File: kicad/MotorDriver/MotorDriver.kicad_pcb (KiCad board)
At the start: 2 copper layers, 74 parts, among them J1 Conn_01x02_Socket, J2 Conn_01x03_Socket, U1 DRV8323RSRGZR, U2 CSD88599Q5DC, U3 CSD88599Q5DC, U5 CSD88599Q5DC, U6 STM32G474RETx

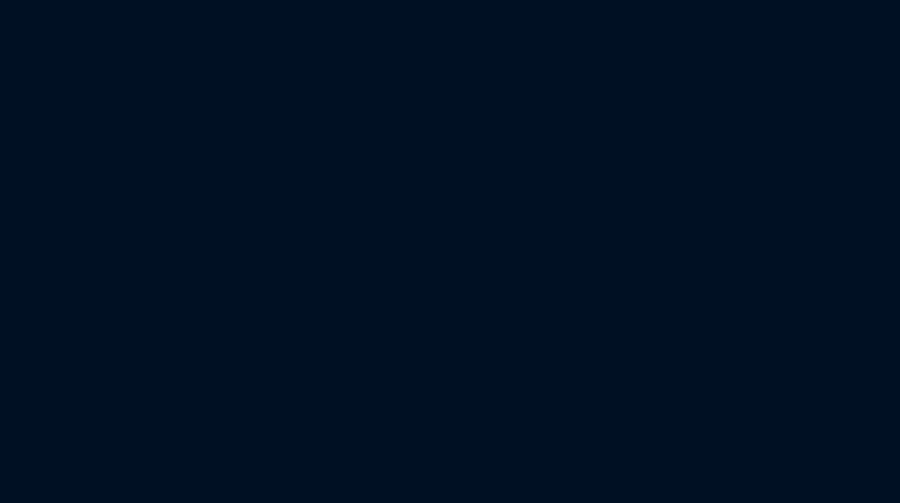
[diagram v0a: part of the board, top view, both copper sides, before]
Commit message: Good progress on the leg prototype. Looking at the jacobian project again, i think I can use some stuff from that project to help size the link lengths and also something to relate the tip forces to joint torques
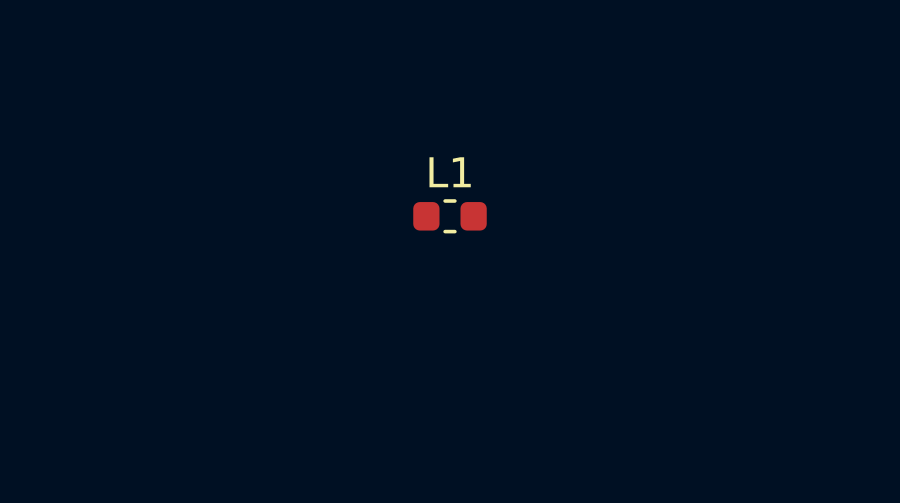
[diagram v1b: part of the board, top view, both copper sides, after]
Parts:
- added L1: L, Inductor_SMD:L_0603_1608Metric, F.Cu at (103.4, 61.0)
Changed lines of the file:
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@@
       (net 42 "/SHC") (pinfunction "2") (pintype "passive"))
+  )
+  (footprint "Inductor_SMD:L_0603_1608Metric" (layer "F.Cu")
+    (at 103.3525 60.96)
+    (descr "Inductor SMD 0603 (1608 Metric), square (rectangular) end terminal, IPC_7351 nominal, (Body size source: http://www.tortai-tech.com/upload/download/2011102023233369053.pdf), generated with kicad-footprint-generator")
+    (tags "inductor")
+    (property "Sheetfile" "MotorDriver.kicad_sch")
+    (property "Sheetname" "")
+    (property "ki_description" "Inductor")
+    (property "ki_keywords" "inductor choke coil reactor magnetic")
+    (attr smd)
+    (fp_text reference "L1" (at 0 -1.43) (layer "F.SilkS")
+        (effects (font (size 1 1) (thickness 0.15)))
+    )
+    (fp_text value "L" (at 0 1.43) (layer "F.Fab")
+        (effects (font (size 1 1) (thickness 0.15)))
+    )
+    (fp_text user "${REFERENCE}" (at 0 0) (layer "F.Fab")
+        (effects (font (size 0.4 0.4) (thickness 0.06)))
+    )
+    (fp_line (start -0.162779 -0.51) (end 0.162779 -0.51)
+      (stroke (width 0.12) (type solid)) (layer "F.SilkS"))
+    (fp_line (start -0.162779 0.51) (end 0.162779 0.51)
+      (stroke (width 0.12) (type solid)) (layer "F.SilkS"))
+    (fp_line (start -1.48 -0.73) (end 1.48 -0.73)
+      (stroke (width 0.05) (type solid)) (layer "F.CrtYd"))
+    (fp_line (start -1.48 0.73) (end -1.48 -0.73)
+      (stroke (width 0.05) (type solid)) (layer "F.CrtYd"))
+    (fp_line (start 1.48 -0.73) (end 1.48 0.73)
+      (stroke (width 0.05) (type solid)) (layer "F.CrtYd"))
+    (fp_line (start 1.48 0.73) (end -1.48 0.73)
+      (stroke (width 0.05) (type solid)) (layer "F.CrtYd"))
+    (fp_line (start -0.8 -0.4) (end 0.8 -0.4)
+      (stroke (width 0.1) (type solid)) (layer "F.Fab"))
+    (fp_line (start -0.8 0.4) (end -0.8 -0.4)
+      (stroke (width 0.1) (type solid)) (layer "F.Fab"))
+    (fp_line (start 0.8 -0.4) (end 0.8 0.4)
+      (stroke (width 0.1) (type solid)) (layer "F.Fab"))
+    (fp_line (start 0.8 0.4) (end -0.8 0.4)
+      (stroke (width 0.1) (type solid)) (layer "F.Fab"))
+    (pad "1" smd roundrect (at -0.7875 0) (size 0.875 0.95) (layers "F.Cu" "F.Paste" "F.Mask") (roundrect_rratio 0.25)
+      (net 48 "Net-(D4-K)") (pinfunction "1") (pintype "passive"))
+    (pad "2" smd roundrect (at 0.7875 0) (size 0.875 0.95) (layers "F.Cu" "F.Paste" "F.Mask") (roundrect_rratio 0.25)
+      (net 17 "+3.3V") (pinfunction "2") (pintype "passive"))
+    (model "${KICAD6_3DMODEL_DIR}/Inductor_SMD.3dshapes/L_0603_1608Metric.wrl"
+      (offset (xyz 0 0 0))
+      (scale (xyz 1 1 1))
+      (rotate (xyz 0 0 0))
+    )
   )
   (footprint "Diode_SMD:D_MELF" (layer "F.Cu")

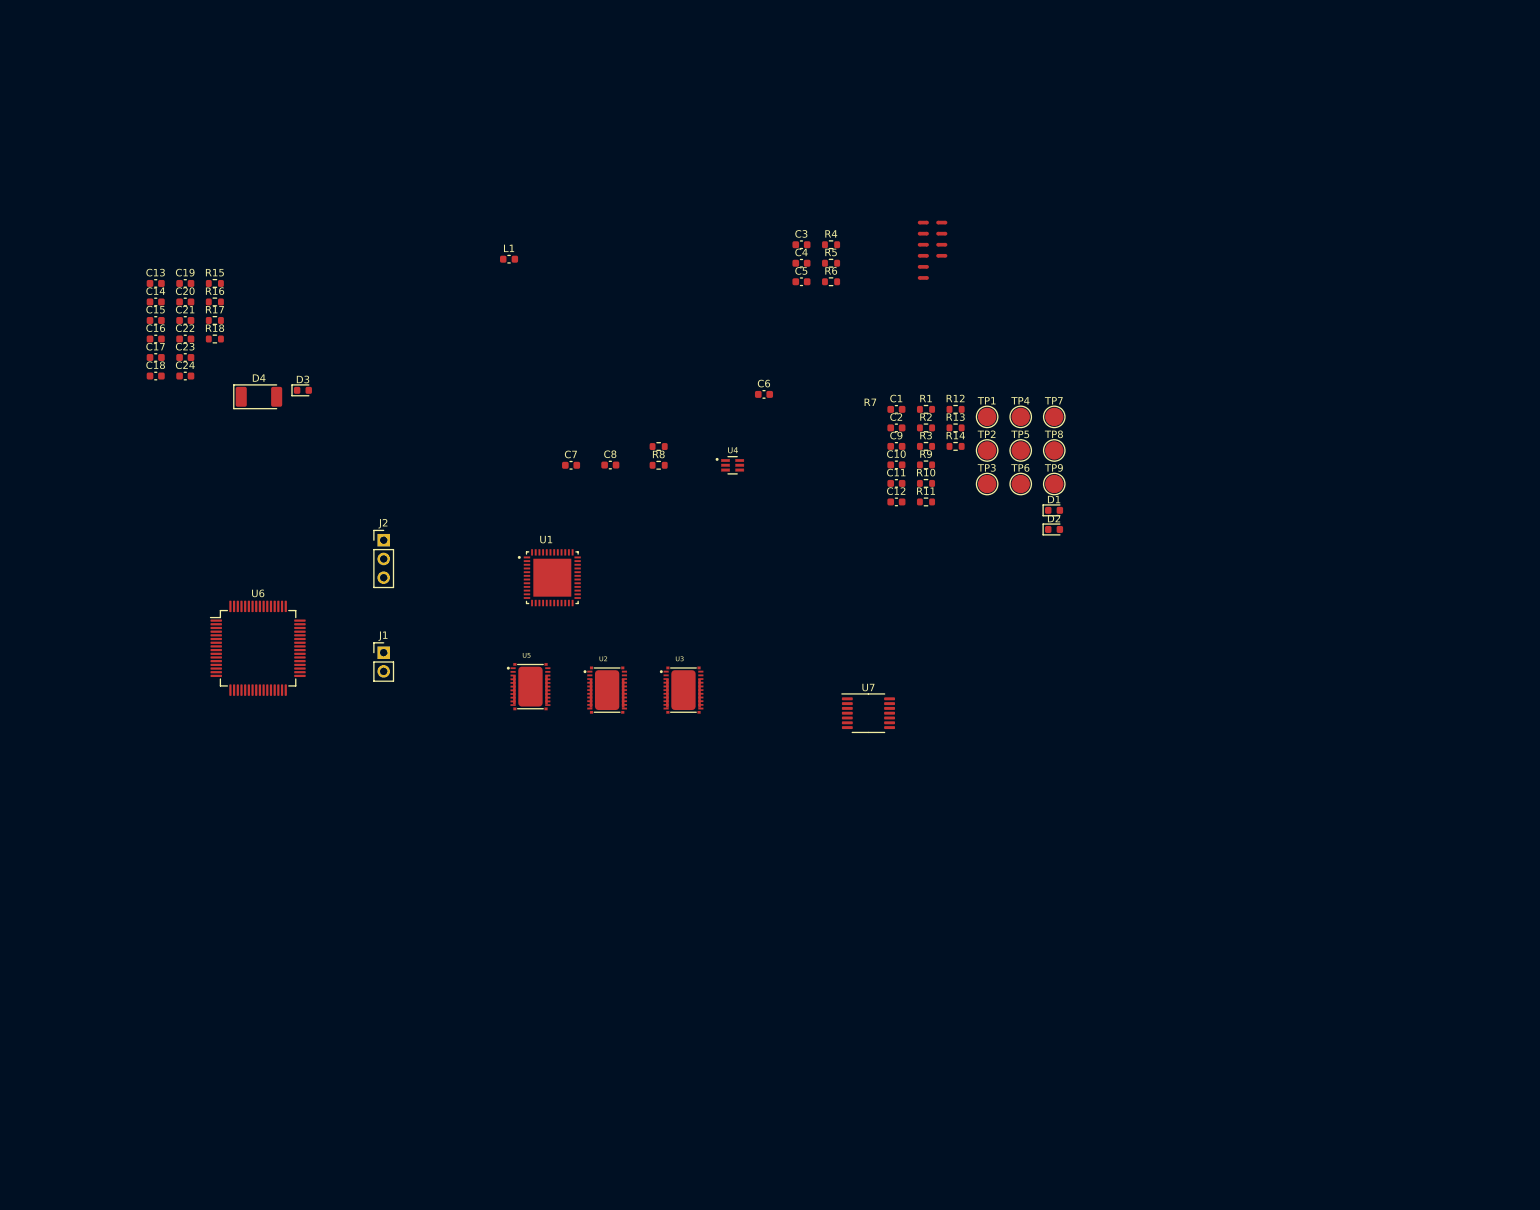
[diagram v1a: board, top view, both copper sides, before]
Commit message: Schematic capture is like 80% complete. There are some components that don't have appropriate footprints, IE the 330 mH caps. Started board layout. I'm not sure if I can fit everything in the current board outline though. I may need to expand to a full circle instead of having the cutout sections.
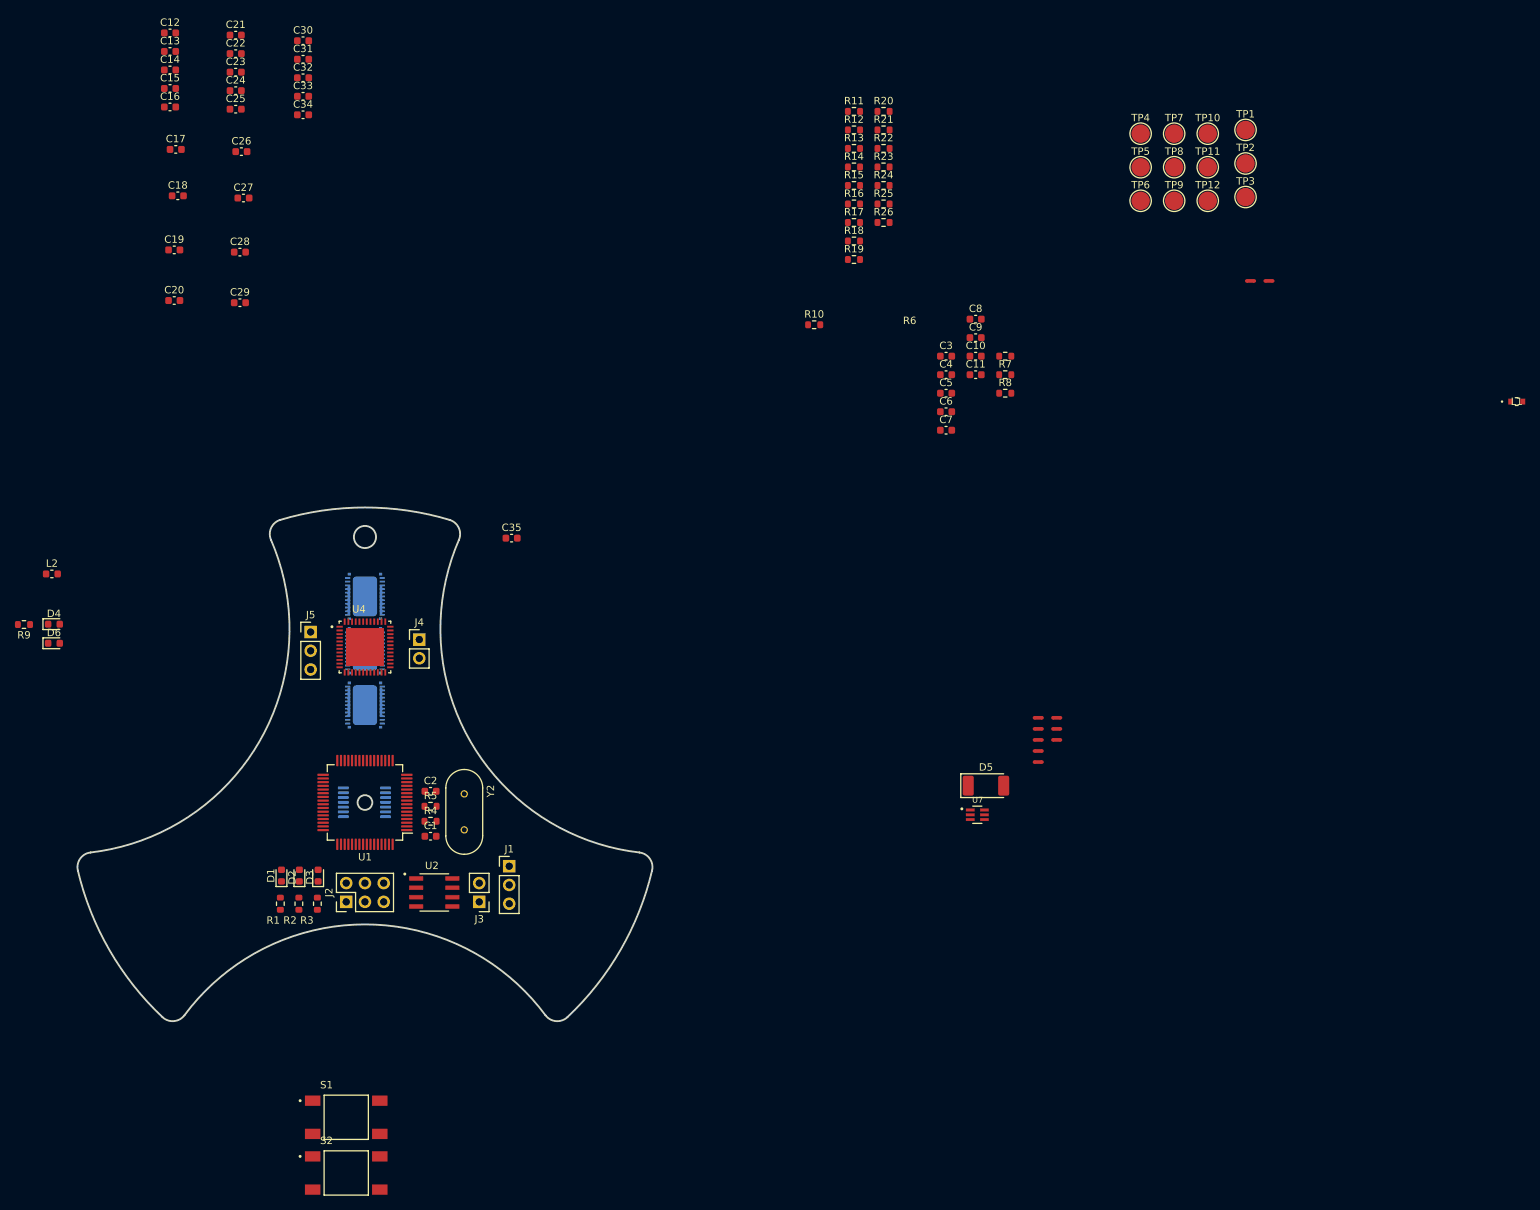
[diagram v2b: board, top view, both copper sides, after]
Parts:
- added C25: 0.1 uF, Capacitor_SMD:C_0603_1608Metric, F.Cu at (66.3, 40.6)
- added C26: 330uF, Capacitor_SMD:C_0603_1608Metric, F.Cu at (67.1, 46.4)
- added C27: 330uF, Capacitor_SMD:C_0603_1608Metric, F.Cu at (67.3, 52.7)
- added C28: 2200pF, Capacitor_SMD:C_0603_1608Metric, F.Cu at (66.9, 60.0)
- added C29: 2200pF, Capacitor_SMD:C_0603_1608Metric, F.Cu at (66.9, 66.9)
- added C30: 0.1uF, Capacitor_SMD:C_0603_1608Metric, F.Cu at (75.4, 31.3)
- added C31: 2200pF, Capacitor_SMD:C_0603_1608Metric, F.Cu at (75.4, 33.9)
- added C32: 0.01 uF, Capacitor_SMD:C_0603_1608Metric, F.Cu at (75.4, 36.4)
- added C33: 0.1 uF, Capacitor_SMD:C_0603_1608Metric, F.Cu at (75.4, 38.9)
- added C34: 0.01 uF, Capacitor_SMD:C_0603_1608Metric, F.Cu at (75.4, 41.4)
- added C35: 0.1 uF, Capacitor_SMD:C_0603_1608Metric, F.Cu at (103.7, 98.8)
- added D5: MBR1H100SFT3G, Diode_SMD:D_MELF, F.Cu at (168.0, 132.3)
- added D6: LED, LED_SMD:LED_0603_1608Metric, F.Cu at (41.7, 113.0)
- added J3: Conn_01x02_Pin, Connector_PinHeader_2.54mm:PinHeader_1x02_P2.54mm_Vertical, F.Cu at (99.3, 148.1)
- added J4: Conn_01x02_Socket, Connector_PinHeader_2.54mm:PinHeader_1x02_P2.54mm_Vertical, F.Cu at (91.2, 112.5)
- added J5: Conn_01x03_Socket, Connector_PinHeader_2.54mm:PinHeader_1x03_P2.54mm_Vertical, F.Cu at (76.5, 111.5)
- added L2: 15uH, Inductor_SMD:L_0603_1608Metric, F.Cu at (41.4, 103.6)
- added R19: 56, Resistor_SMD:R_0603_1608Metric, F.Cu at (150.1, 61.0)
- added R20: 56, Resistor_SMD:R_0603_1608Metric, F.Cu at (154.1, 40.9)
- added R21: 82.0k, Resistor_SMD:R_0603_1608Metric, F.Cu at (154.1, 43.4)
- added R22: 4.99k, Resistor_SMD:R_0603_1608Metric, F.Cu at (154.1, 45.9)
- added R23: 0.007, Resistor_SMD:R_0603_1608Metric, F.Cu at (154.1, 48.5)
- added R24: 82.0k, Resistor_SMD:R_0603_1608Metric, F.Cu at (154.1, 51.0)
- added R25: 4.99k, Resistor_SMD:R_0603_1608Metric, F.Cu at (154.1, 53.5)
- added R26: 0.007, Resistor_SMD:R_0603_1608Metric, F.Cu at (154.1, 56.0)
- added S1: TS04-66-75-BK-160-SMT, TylerLib:SW_TS04-66-75-BK-160-SMT, F.Cu at (81.3, 177.3)
- added S2: TS04-66-75-BK-160-SMT, TylerLib:SW_TS04-66-75-BK-160-SMT, F.Cu at (81.3, 184.8)
- added TP10: TestPoint, TestPoint:TestPoint_Pad_D2.5mm, F.Cu at (198.1, 43.9)
- added TP11: TestPoint, TestPoint:TestPoint_Pad_D2.5mm, F.Cu at (198.1, 48.5)
- added TP12: TestPoint, TestPoint:TestPoint_Pad_D2.5mm, F.Cu at (198.1, 53.0)
- added U8: CSD88599Q5DC, TylerLib:MOSFET_CSD88599Q5DC, B.Cu at (83.8, 121.4)
- added Y2: ABL-8.000MHZ-B1U-T, TylerLib:XTAL_ABL-8.000MHZ-B1U-T, F.Cu at (97.3, 135.9)
- C1: value 0.01 uF -> 18pF
- C10: value 0.1 uF -> 100nF
- C11: value 0.01 uF -> 100nF
- C12: value 0.1 uF -> 0.1uF
- C13: value 2.2uF -> 4.7uF
- C14: value 0.1uF -> 2.2uF
- C15, C21: value 1uF -> 0.1uF
- C16: value 0.047uF -> 1uF
- C18: value 1uF -> 0.047uF
- C19, C20, C22: value 1uF -> 1000pF
- C2: value 0.1 uF -> 18pF
- C23: value 1uF -> 22uF
- C24: value 22uF -> 0.01 uF
- C3, C4: value 330uF -> 100nF
- C5, C6, C8: value 2200pF -> 100nF
- C7: value 0.1uF -> 100nF
- C9: value 0.01 uF -> 4.7uF
- D4: value 1N6857UR -> LED; footprint Diode_SMD:D_MELF -> LED_SMD:LED_0603_1608Metric
- J1: value Conn_01x02_Socket -> Conn_01x03_Pin; footprint Connector_PinHeader_2.54mm:PinHeader_1x02_P2.54mm_Vertical -> Connector_PinHeader_2.54mm:PinHeader_1x03_P2.54mm_Vertical
- J2: value Conn_01x03_Socket -> Conn_01x06_Pin; footprint Connector_PinHeader_2.54mm:PinHeader_1x03_P2.54mm_Vertical -> Connector_PinHeader_2.54mm:PinHeader_2x03_P2.54mm_Vertical
- L1: value L -> MMZ1608B601CTAH0; footprint Inductor_SMD:L_0603_1608Metric -> TylerLib:IND_1608_TDK
- R1: value 82.0k -> 1k
- R10: value 4.99k -> 10k
- R11: value 0.007 -> 28.0k
- R12: value 82.0k -> 8.45k
- R13: value 4.99k -> 82.0k
- R14: value 0.007 -> 4.99k
- R15: value 330 -> 0.007
- R16: value 10k -> 82.0k
- R17: value 28.0k -> 4.99k
- R18: value 8.45k -> 56
- R2: value 4.99k -> 1k
- R3: value 0.007 -> 1k
- R4: value 82.0k -> 80
- R5: value 4.99k -> 80
- R6: value 56 -> 10k
- R7: value 56 -> 4.7k
- R8: value 56 -> 100
- R9: value 82.0k -> 330
- U1: value DRV8323RSRGZR -> STM32F446RETx; footprint TylerLib:QFN50P700X700X100-49N -> Package_QFP:LQFP-64_10x10mm_P0.5mm
- U2: value CSD88599Q5DC -> ATA6560-GAQW; footprint TylerLib:MOSFET_CSD88599Q5DC -> TylerLib:SOIC127P600X175-8N
- U3: value CSD88599Q5DC -> AS5147U; footprint TylerLib:MOSFET_CSD88599Q5DC -> Package_SO:TSSOP-14_4.4x5mm_P0.65mm; moved to B.Cu
- U4: value ~ -> DRV8323RSRGZR; footprint TylerLib:SOT65P210X110-6N -> TylerLib:QFN50P700X700X100-49N
- U5: moved to B.Cu
- U6: value STM32G474RETx -> CSD88599Q5DC; footprint Package_QFP:LQFP-64_10x10mm_P0.5mm -> TylerLib:MOSFET_CSD88599Q5DC; moved to B.Cu
- U7: footprint Package_SO:TSSOP-14_4.4x5mm_P0.65mm -> TylerLib:SOT65P210X110-6N
- moved L1 138.0 mm to (240.0, 80.3)
- moved R9 124.2 mm to (37.6, 110.5), turned to 180 degrees
- moved C12 117.2 mm to (57.4, 30.3)
- moved D1 115.9 mm to (72.5, 144.5), turned to 90 degrees
- moved D2 112.6 mm to (74.9, 144.5), turned to 90 degrees
- moved R1 110.2 mm to (72.3, 148.3), turned to -90 degrees
- moved R2 106.7 mm to (74.9, 148.3), turned to -90 degrees
- moved R3 103.2 mm to (77.4, 148.3), turned to -90 degrees
- moved R4 95.2 mm to (92.7, 137.2)
- moved R5 91.5 mm to (92.7, 135.1)
- moved R15 87.7 mm to (150.1, 51.0)
- moved R16 87.7 mm to (150.1, 53.5)
- moved R18 87.7 mm to (150.1, 58.5)
- moved R17 87.7 mm to (150.1, 56.0)
- moved C1 85.7 mm to (92.7, 139.2)
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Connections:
- C1 pad 1: Vdrive -> GND
- C1 pad 2: /SLA -> Net-(C1-Pad2)
- C10 pad 1: /VSENB -> Net-(C10-Pad1)
- C10 pad 2: GND -> /Microcontroller/NRST
- C11 pad 1: Vdrive -> Net-(C11-Pad1)
- C11 pad 2: /SLC -> /Microcontroller/Button
- C12 pad 1: /VSENC -> +3.3V
- C14 pad 1: +3.3V -> Vdrive
- C15 pad 1: Net-(U1-DVDD) -> Vdrive
- C16 pad 1: Net-(U1-CPH) -> Net-(U4-DVDD)
- C16 pad 2: Net-(U1-CPL) -> GND
- C17 pad 2: Net-(U1-VCP) -> Net-(U4-VCP)
- C18 pad 1: Vdrive -> Net-(U4-CPH)
- C18 pad 2: GND -> Net-(U4-CPL)
- C19 pad 1: Vdrive -> /MotorController/SPC
- C19 pad 2: GND -> /MotorController/SNC
- C2 pad 1: /VSENA -> GND
- C2 pad 2: GND -> Net-(C2-Pad2)
- C20 pad 1: /SPC -> /MotorController/SPA
- C20 pad 2: /SNC -> /MotorController/SNA
- C21 pad 1: /SPB -> Net-(U4-CB)
- C21 pad 2: /SNB -> Net-(D5-K)
- C22 pad 1: /SPA -> /MotorController/SPB
- C22 pad 2: /SNA -> /MotorController/SNB
- C23 pad 1: Net-(U1-CB) -> +3.3V
- C23 pad 2: Net-(D4-K) -> GND
- C24 pad 1: +3.3V -> Vdrive
- C24 pad 2: GND -> /MotorController/SLA
- C3 pad 1: Net-(J1-Pin_1) -> GND
- C3 pad 2: GND -> +3.3V
- C4 pad 1: Net-(J1-Pin_1) -> GND
- C4 pad 2: GND -> +3.3V
- C5 pad 1: /ISENA -> GND
- C5 pad 2: GND -> +3.3V
- C6 pad 1: /ISENB -> GND
- C6 pad 2: GND -> +3.3V
- C7 pad 1: Net-(C7-Pad1) -> GND
- C7 pad 2: GND -> +3.3V
- C8 pad 1: /ISENC -> GND
- C8 pad 2: GND -> +3.3V
- C9 pad 1: Vdrive -> GND
- C9 pad 2: /SLB -> Net-(U1-VCAP_1)
- D1 pad 1: GND -> Net-(D1-K)
- D1 pad 2: +3.3V -> Net-(D1-A)
- D2 pad 1: GND -> Net-(D2-K)
- D2 pad 2: /LED -> Net-(D2-A)
- D3 pad 2: +3.3V -> Net-(D3-A)
- D4 pad 2: GND -> +3.3V
- J1 pad 1: Net-(J1-Pin_1) -> GND
- J1 pad 2: GND -> /Microcontroller/UART_RX
- J2 pad 1: /MOTA -> /Microcontroller/NRST
- J2 pad 2: /MOTB -> /Microcontroller/TCK
- J2 pad 3: /MOTC -> /Microcontroller/TMS
- L1 pad 1: Net-(D4-K) -> Net-(U1-VDDA)
- NT1 pad 1: /SPA -> /MotorController/SPA
- NT1 pad 2: /SLA -> /MotorController/SLA
- NT10 pad 1: Net-(U5-SH) -> Net-(U8-SH)
- NT10 pad 2: /SHC -> /MotorController/SHC
- NT2 pad 1: /SNA -> /MotorController/SNA
- NT3 pad 1: Net-(U2-SH) -> Net-(U5-SH)
- NT3 pad 2: /SHA -> /MotorController/SHA
- NT4 pad 1: /VDRAIN -> /MotorController/VDRAIN
- NT5 pad 1: /SPB -> /MotorController/SPB
- NT5 pad 2: /SLB -> /MotorController/SLB
- NT6 pad 1: /SNB -> /MotorController/SNB
- NT7 pad 1: Net-(U3-SH) -> Net-(U6-SH)
- NT7 pad 2: /SHB -> /MotorController/SHB
- NT8 pad 1: /SPC -> /MotorController/SPC
- NT8 pad 2: /SLC -> /MotorController/SLC
- NT9 pad 1: /SNC -> /MotorController/SNC
- R1 pad 1: /MOTA -> Net-(D1-K)
- R1 pad 2: /VSENA -> GND
- R10 pad 1: /VSENB -> +3.3V
- R10 pad 2: GND -> /MotorController/nFault
- R11 pad 1: /SLB -> +3.3V
- R11 pad 2: GND -> Net-(U4-FB)
- R12 pad 1: /MOTC -> Net-(U4-FB)
- R12 pad 2: /VSENC -> GND
- R13 pad 1: /VSENC -> /MotorController/MOTA
- R13 pad 2: GND -> /MotorController/SEN.VSENA
- R14 pad 1: /SLC -> /MotorController/SEN.VSENA
- R15 pad 1: Net-(D3-K) -> /MotorController/SLA
- R15 pad 2: /nFault -> GND
- R16 pad 1: +3.3V -> Net-(J4-Pin_1)
- R16 pad 2: /nFault -> /MotorController/SEN.VSENVM
- R17 pad 1: +3.3V -> /MotorController/SEN.VSENVM
- R17 pad 2: Net-(U1-FB) -> GND
- R18 pad 1: Net-(U1-FB) -> /MotorController/SOA
- R18 pad 2: GND -> /MotorController/ISENA
- R2 pad 1: /VSENA -> Net-(D2-K)
- R3 pad 1: /SLA -> Net-(D3-K)
- R4 pad 1: Net-(J1-Pin_1) -> Net-(U1-PH0)
- R4 pad 2: Net-(C7-Pad1) -> Net-(C1-Pad2)
- R5 pad 1: Net-(C7-Pad1) -> Net-(U1-PH1)
- R5 pad 2: GND -> Net-(C2-Pad2)
- R6 pad 1: /SOA -> /Microcontroller/BOOT0
- R6 pad 2: /ISENA -> GND
- R7 pad 1: /SOB -> +3.3V
- R7 pad 2: /ISENB -> /Microcontroller/Button
- R8 pad 1: /SOC -> Net-(C11-Pad1)
- R8 pad 2: /ISENC -> Net-(R8-Pad2)
- R9 pad 1: /MOTB -> Net-(D4-K)
- R9 pad 2: /VSENB -> /MotorController/nFault
- TP1 pad 1: /MOTA -> /Microcontroller/BOOT0
- TP2 pad 1: /GHA -> Net-(U1-PH0)
- TP3 pad 1: /GLA -> /Microcontroller/NRST
- TP4 pad 1: /MOTB -> /MotorController/MOTA
- TP5 pad 1: /GHB -> /MotorController/GHA
- TP6 pad 1: /GLB -> /MotorController/GLA
- TP7 pad 1: /MOTC -> /MotorController/MOTB
- TP8 pad 1: /GHC -> /MotorController/GHB
- TP9 pad 1: /GLC -> /MotorController/GLB
- U1 pad 1: Net-(U1-FB) -> +3.3V
- U1 pad 10: /GLA -> unconnected-(U1-PC2-Pad10)
- U1 pad 11: /SPA -> /Microcontroller/SEN.VSENA
- U1 pad 12: /SNA -> GND
- U1 pad 13: /SNB -> Net-(U1-VDDA)
- U1 pad 14: /SPB -> /Microcontroller/SEN.SOA
- U1 pad 15: /GLB -> /Microcontroller/SEN.VSENVM
- U1 pad 16: /SHB -> /Microcontroller/UART_TX
- U1 pad 17: /GHB -> /Microcontroller/UART_RX
- U1 pad 18: /GHC -> GND
- U1 pad 19: /SHC -> +3.3V
- U1 pad 2: GND -> /Microcontroller/Button
- U1 pad 20: /GLC -> /Microcontroller/SPI1.CS
- U1 pad 21: /SPC -> /Microcontroller/SPI1.SCK
- U1 pad 22: /SNC -> /Microcontroller/SPI1.MISO
- U1 pad 23: /SOC -> /Microcontroller/SPI1.MOSI
- U1 pad 24: /SOB -> /Microcontroller/SEN.VSENB
- U1 pad 25: /SOA -> /Microcontroller/SEN.VSENC
- U1 pad 26: +3.3V -> unconnected-(U1-PB0-Pad26)
- U1 pad 27: GND -> unconnected-(U1-PB1-Pad27)
- U1 pad 28: /nFault -> unconnected-(U1-PB2-Pad28)
- U1 pad 29: /SDO -> unconnected-(U1-PB10-Pad29)
- U1 pad 3: Net-(U1-CPL) -> /Microcontroller/DRV.ENABLE
- U1 pad 30: /SDI -> Net-(U1-VCAP_1)
- U1 pad 31: /SCLK -> GND
- U1 pad 32: /nSCS -> +3.3V
- U1 pad 33: /ENABLE -> unconnected-(U1-PB12-Pad33)
- U1 pad 34: /CAL -> /Microcontroller/DRV.INHA
- U1 pad 35: GND -> /Microcontroller/DRV.INHB
- U1 pad 36: Net-(U1-DVDD) -> /Microcontroller/DRV.INHC
- U1 pad 37: /INHA -> unconnected-(U1-PC6-Pad37)
- U1 pad 38: /INLA -> Net-(D1-A)
- U1 pad 39: /INHB -> Net-(D2-A)
- U1 pad 4: Net-(U1-CPH) -> unconnected-(U1-PC15-Pad4)
- U1 pad 40: /INLB -> Net-(D3-A)
- U1 pad 41: /INHC -> /Microcontroller/DRV.INHA
- U1 pad 42: /INLC -> /Microcontroller/DRV.INHB
- U1 pad 43: GND -> /Microcontroller/DRV.INHC
- U1 pad 44: Net-(U1-CB) -> unconnected-(U1-PA11-Pad44)
- U1 pad 45: Net-(D4-K) -> unconnected-(U1-PA12-Pad45)
- U1 pad 46: unconnected-(U1-NC-Pad46) -> /Microcontroller/TMS
- U1 pad 47: Vdrive -> GND
- U1 pad 48: Vdrive -> +3.3V
- U1 pad 49: GND -> /Microcontroller/TCK
- U1 pad 5: Net-(U1-VCP) -> Net-(U1-PH0)
- U1 pad 6: Vdrive -> Net-(U1-PH1)
- U1 pad 7: /VDRAIN -> /Microcontroller/NRST
- U1 pad 8: /GHA -> /Microcontroller/SEN.SOC
- U1 pad 9: /SHA -> /Microcontroller/SEN.SOB
- U2 pad 1: /GHA -> /Microcontroller/CAN2_TX
- U2 pad 2: Net-(U2-SH) -> GND
- U2 pad 3: /MOTA -> +3.3V
- U2 pad 4: /MOTA -> /Microcontroller/CAN2_RX
- U2 pad 5: /MOTA -> /Microcontroller/CAN2_Silent
- U2 pad 6: /MOTA -> Net-(J3-Pin_1)
- U2 pad 7: /MOTA -> Net-(J3-Pin_2)
- U2 pad 8: /MOTA -> /Microcontroller/CAN2_Standby
- U3 pad 1: /GHB -> /Encoder/SPI3.CS
- U3 pad 10: /MOTB -> unconnected-(U3-U-Pad10)
- U3 pad 11: /MOTB -> +3.3V
- U3 pad 12: /SLB -> +3.3V
- U3 pad 13: /SLB -> GND
- U3 pad 14: /SLB -> /Encoder/M1_ENC.I
- U3 pad 2: Net-(U3-SH) -> /Encoder/SPI3.SCK
- U3 pad 3: /MOTB -> /Encoder/SPI3.MISO
- U3 pad 4: /MOTB -> /Encoder/SPI3.MOSI
- U3 pad 5: /MOTB -> unconnected-(U3-TEST-Pad5)
- U3 pad 6: /MOTB -> /Encoder/M1_ENC.B
- U3 pad 7: /MOTB -> /Encoder/M1_ENC.A
- U3 pad 8: /MOTB -> unconnected-(U3-W/PWM-Pad8)
- U3 pad 9: /MOTB -> unconnected-(U3-V-Pad9)
- U4 pad 1: /VSENA -> Net-(U4-FB)
- U4 pad 3: /VSENB -> Net-(U4-CPL)
- U4 pad 4: /VSENC -> Net-(U4-CPH)
- U4 pad 5: +3.3V -> Net-(U4-VCP)
- U4 pad 6: /VSENVM -> Vdrive
- U5 pad 1: /GHC -> /MotorController/GHA
- U5 pad 10: /MOTC -> /MotorController/MOTA
- U5 pad 11: /MOTC -> /MotorController/MOTA
- U5 pad 12: /SLC -> /MotorController/SLA
- U5 pad 13: /SLC -> /MotorController/SLA
- U5 pad 14: /SLC -> /MotorController/SLA
- U5 pad 15: /SLC -> /MotorController/SLA
- U5 pad 16: /SLC -> /MotorController/SLA
- U5 pad 17: /SLC -> /MotorController/SLA
- U5 pad 18: /SLC -> /MotorController/SLA
- U5 pad 19: /SLC -> /MotorController/SLA
- U5 pad 20: /SLC -> /MotorController/SLA
- U5 pad 21: (no net) -> unconnected-(U5-NC-Pad21)
- U5 pad 22: /GLC -> /MotorController/GLA
- U5 pad 23: (no net) -> unconnected-(U5-NC-Pad23)
- U5 pad 24: (no net) -> unconnected-(U5-NC-Pad24)
- U5 pad 25: (no net) -> unconnected-(U5-NC-Pad25)
- U5 pad 26: (no net) -> unconnected-(U5-NC-Pad26)
- U5 pad 3: /MOTC -> /MotorController/MOTA
- U5 pad 4: /MOTC -> /MotorController/MOTA
- U5 pad 5: /MOTC -> /MotorController/MOTA
- U5 pad 6: /MOTC -> /MotorController/MOTA
- U5 pad 7: /MOTC -> /MotorController/MOTA
- U5 pad 8: /MOTC -> /MotorController/MOTA
- U5 pad 9: /MOTC -> /MotorController/MOTA
- U6 pad 1: unconnected-(U6-VBAT-Pad1) -> /MotorController/GHB
- U6 pad 10: unconnected-(U6-PC2-Pad10) -> /MotorController/MOTB
- U6 pad 11: unconnected-(U6-PC3-Pad11) -> /MotorController/MOTB
- U6 pad 12: unconnected-(U6-PA0-Pad12) -> /MotorController/SLB
- U6 pad 13: unconnected-(U6-PA1-Pad13) -> /MotorController/SLB
- U6 pad 14: unconnected-(U6-PA2-Pad14) -> /MotorController/SLB
- U6 pad 15: Net-(U6-VSS-Pad15) -> /MotorController/SLB
- U6 pad 16: unconnected-(U6-VDD-Pad16) -> /MotorController/SLB
- U6 pad 17: unconnected-(U6-PA3-Pad17) -> /MotorController/SLB
- U6 pad 18: unconnected-(U6-PA4-Pad18) -> /MotorController/SLB
- U6 pad 19: unconnected-(U6-PA5-Pad19) -> /MotorController/SLB
- U6 pad 2: unconnected-(U6-PC13-Pad2) -> Net-(U6-SH)
- U6 pad 20: unconnected-(U6-PA6-Pad20) -> /MotorController/SLB
- U6 pad 22: unconnected-(U6-PC4-Pad22) -> /MotorController/GLB
- U6 pad 27: unconnected-(U6-VSSA-Pad27) -> Vdrive
- U6 pad 3: unconnected-(U6-PC14-Pad3) -> /MotorController/MOTB
- U6 pad 4: unconnected-(U6-PC15-Pad4) -> /MotorController/MOTB
- U6 pad 5: unconnected-(U6-PF0-Pad5) -> /MotorController/MOTB
- U6 pad 6: unconnected-(U6-PF1-Pad6) -> /MotorController/MOTB
- U6 pad 7: unconnected-(U6-PG10-Pad7) -> /MotorController/MOTB
- U6 pad 8: unconnected-(U6-PC0-Pad8) -> /MotorController/MOTB
- U6 pad 9: unconnected-(U6-PC1-Pad9) -> /MotorController/MOTB
- U7 pad 1: unconnected-(U7-CSn-Pad1) -> /MotorController/VSENA
- U7 pad 2: unconnected-(U7-CLK-Pad2) -> GND
- U7 pad 3: unconnected-(U7-MISO-Pad3) -> /MotorController/VSENB
- U7 pad 4: unconnected-(U7-MOSI-Pad4) -> /MotorController/VSENC
- U7 pad 5: unconnected-(U7-TEST-Pad5) -> +3.3V
- U7 pad 6: unconnected-(U7-B-Pad6) -> /MotorController/VSENVM
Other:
- board outline added: 78 x 69.6 mm

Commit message: Pushing before the drive to Boston...
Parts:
- U5, U6, U8: moved to F.Cu
- moved L1 155.9 mm to (92.7, 131.3)
- moved S1 153.5 mm to (225.0, 123.4), turned to 45 degrees
- moved C6 104.7 mm to (74.4, 138.2), turned to -90 degrees
- moved C3 96.7 mm to (92.7, 141.0), turned to 180 degrees
- moved C8 95.5 mm to (92.7, 129.5), turned to 180 degrees
- moved C5 94.6 mm to (80.3, 125.7), turned to 180 degrees
- moved C7 91.2 mm to (92.7, 142.7), turned to 180 degrees
- moved C4 90.3 mm to (86.9, 125.7), turned to 180 degrees
- moved J4 24.3 mm to (98.8, 89.4)
- moved S2 24.0 mm to (66.3, 166.1)
- moved J5 22.4 mm to (66.5, 91.4)
- moved U8 16.8 mm to (83.8, 104.6), turned to 180 degrees
- moved U6 12.8 mm to (73.6, 106.4), turned to 180 degrees
- moved U5 10.3 mm to (94.1, 106.4), turned to 0 degrees
- moved J1 9.91 mm to (112.5, 147.1)
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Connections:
- C8 pad 2: +3.3V -> /Microcontroller/VDDA
- L1 pad 1: Net-(U1-VDDA) -> /Microcontroller/VDDA
- U1 pad 13: Net-(U1-VDDA) -> /Microcontroller/VDDA
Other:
- copper layers 2 -> 4
